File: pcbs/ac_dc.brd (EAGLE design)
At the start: 94 x 20 mm, 19 parts, among them IC1 317T, J1 22-27-2021-02, K1 G6K-2F

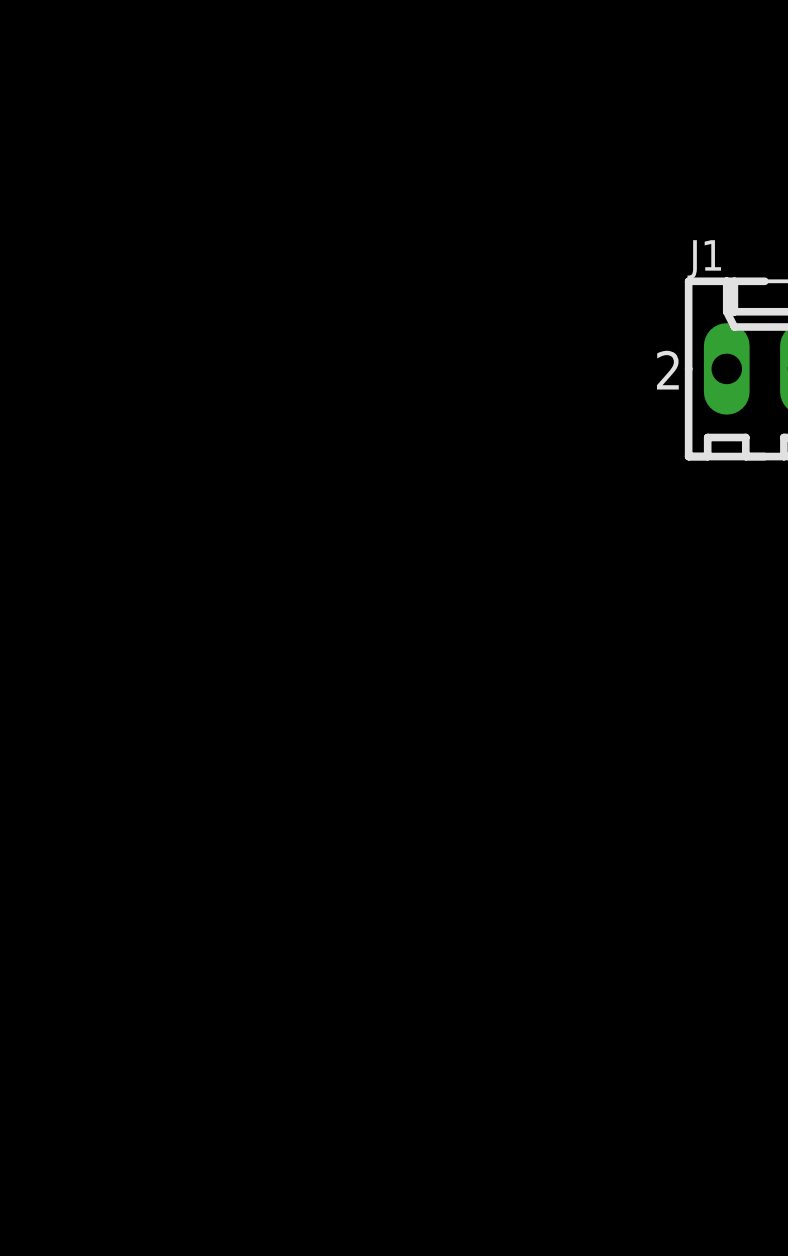
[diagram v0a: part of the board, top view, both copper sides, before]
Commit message: AC/DC: Added atmega88 and power supply.
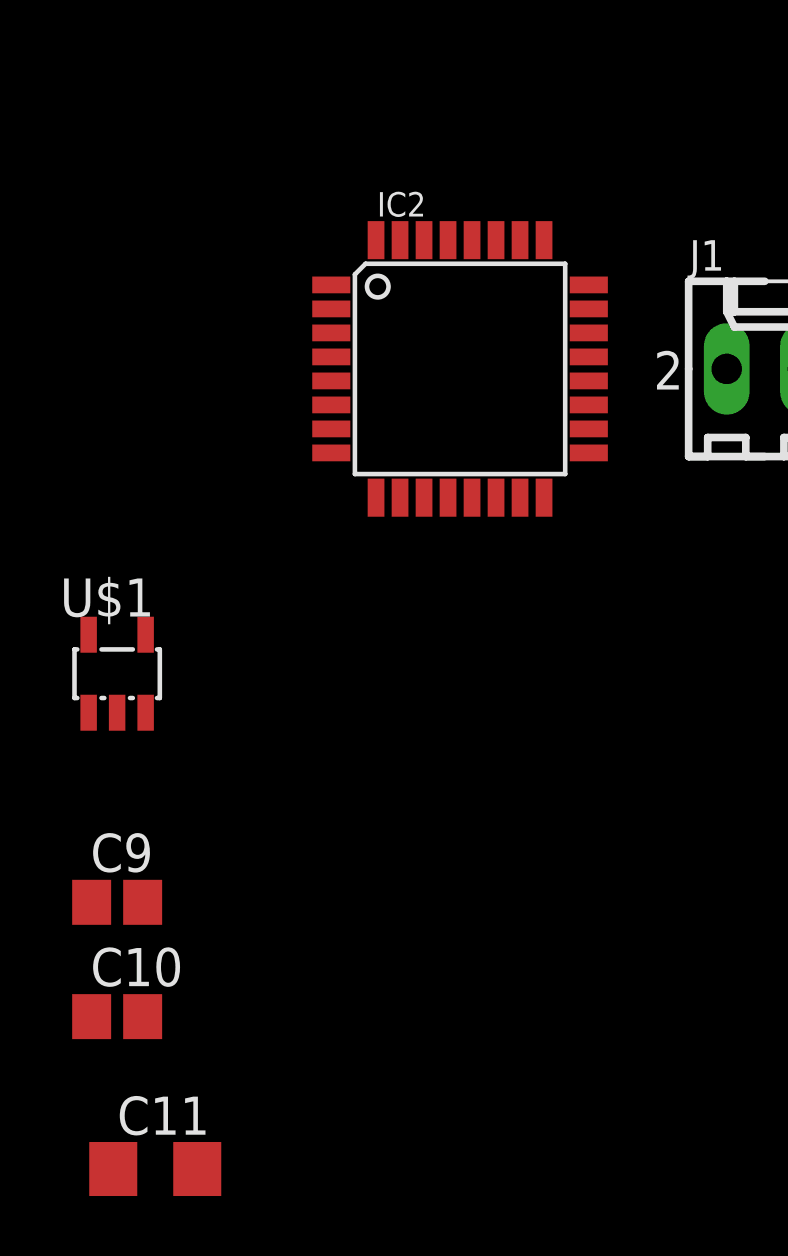
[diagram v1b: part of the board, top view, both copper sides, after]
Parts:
- added C10, C9: 100n, resistor:C0805
- added C11: 10u, resistor:C1206
- added IC2: MEGA48/88/168-AU, avr-7:TQFP32-08
- added U$1: TPS71530, ShortCircuitRobotics:SOT23-DBV
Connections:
- removed net N$15: C8.+, IC1.2
- new net +12V: C8.+, IC1.2, U$1.4
- new net VCC: C10.1, C11.1, C9.1, IC2.18, IC2.20, IC2.4, IC2.6, U$1.5
- net GND: now also C10.2, C11.2, C9.2, IC2.21, IC2.3, IC2.5, U$1.2
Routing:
- net N$15: track 13.4 -> 0.00 mm
- net +12V: track 0.00 -> 13.4 mm

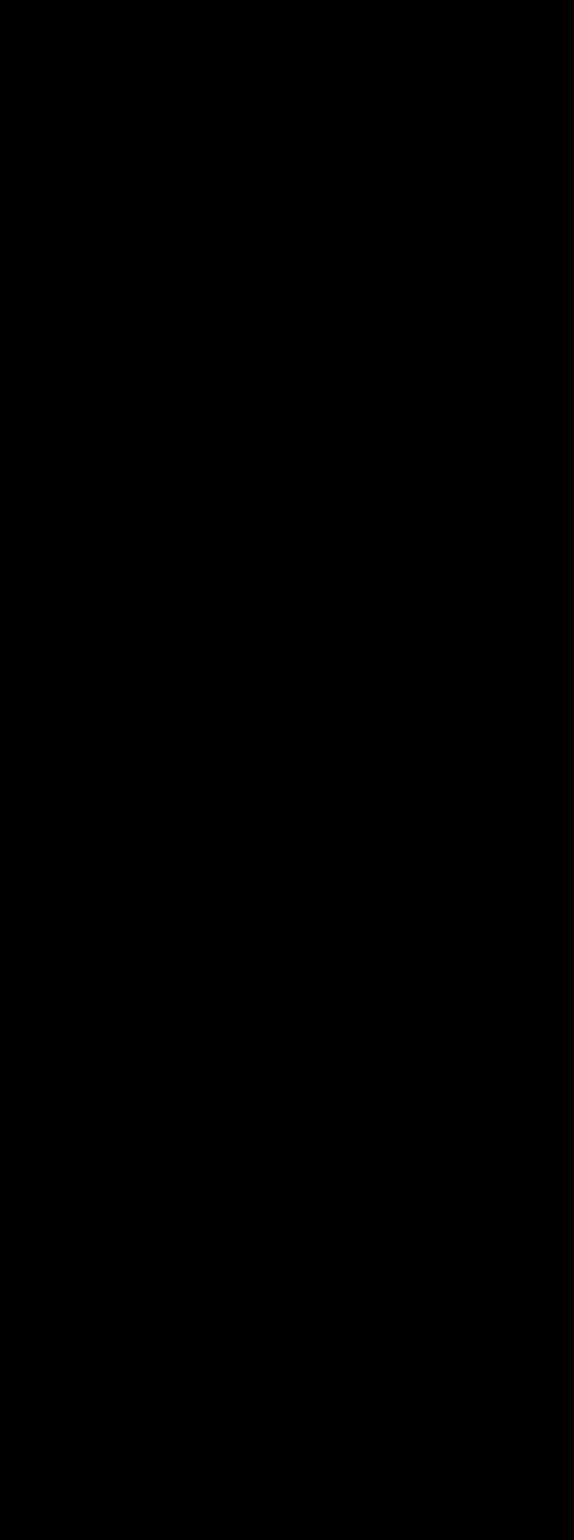
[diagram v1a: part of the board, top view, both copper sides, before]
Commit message: Main Board: Added battery connector + mosfet switch
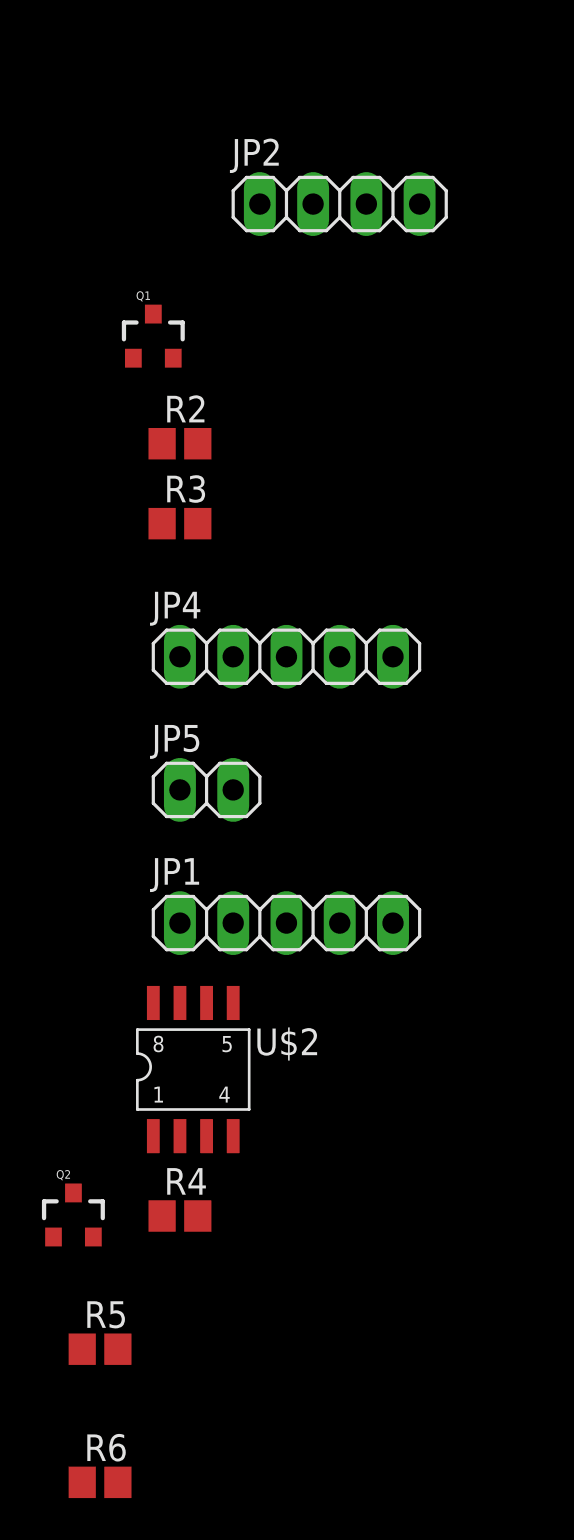
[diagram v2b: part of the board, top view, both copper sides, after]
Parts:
- added JP1, JP4: (no value), pinhead:1X05
- added JP2: (no value), pinhead:1X04
- added JP5: (no value), pinhead:1X02
- added Q1, Q2: MOSFET-NCHANNELSMD, SparkFun:SOT23-3
- added R2, R4, R5: 100k, resistor:R0805
- added R3, R6: 1k, resistor:R0805
- added U$2: IRF7416, ShortCircuitRobotics:SO8-2
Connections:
- new net BATTERY_ON: R6.1
- new net CELL_0: JP4.4
- new net CELL_1: JP4.3
- new net CELL_2: JP4.2
- new net CELL_3: JP4.1, U$2.5, U$2.6, U$2.7, U$2.8
- new net INPUT_SEL: R3.1
- new net N$11: JP1.3
- new net N$12: JP1.4
- new net N$14: K1.8, Q1.3
- new net N$15: Q1.1, R2.2, R3.2
- new net N$16: Q2.3, R4.1, U$2.4
- new net N$17: Q2.1, R5.1, R6.2
- new net N$7: JP1.2
- new net SPEED_REAR_IN: JP5.1
- new net SPEED_REAR_OUT: JP5.2
- net +12V: now also JP1.1, K1.1, R4.2, U$2.1, U$2.2, U$2.3
- net GND: now also JP1.5, JP4.5, Q1.2, Q2.2, R2.1, R5.2
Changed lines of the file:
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@@
 <element name="C10" library="resistor" package="C0805" value="100n" x="-38.1" y="-26.67"/>
 <element name="C11" library="resistor" package="C1206" value="10u" x="-36.83" y="-31.75"/>
+<element name="JP2" library="pinhead" package="1X04" value="" x="-34.29" y="-45.72"/>
+<element name="Q1" library="SparkFun" package="SOT23-3" value="MOSFET-NCHANNELSMD" x="-43.18" y="-52.07"/>
+<element name="R2" library="resistor" package="R0805" value="100k" x="-41.91" y="-57.15"/>
+<element name="R3" library="resistor" package="R0805" value="1k" x="-41.91" y="-60.96"/>
+<element name="JP4" library="pinhead" package="1X05" value="" x="-36.83" y="-67.31"/>
+<element name="JP5" library="pinhead" package="1X02" value="" x="-40.64" y="-73.66"/>
+<element name="JP1" library="pinhead" package="1X05" value="" x="-36.83" y="-80.01"/>
+<element name="U$2" library="ShortCircuitRobotics" package="SO8-2" value="IRF7416" x="-40.64" y="-87.63"/>
+<element name="R4" library="resistor" package="R0805" value="100k" x="-41.91" y="-93.98"/>
+<element name="Q2" library="SparkFun" package="SOT23-3" value="MOSFET-NCHANNELSMD" x="-46.99" y="-93.98"/>
+<element name="R5" library="resistor" package="R0805" value="100k" x="-45.72" y="-100.33"/>
+<element name="R6" library="resistor" package="R0805" value="1k" x="-45.72" y="-106.68"/>
 </elements>
 <signals>
@@
 <contactref element="C9" pad="2"/>
 <contactref element="C10" pad="2"/>
-<wire x1="46.03" y1="13.97" x2="66.88" y2="2.54" width="0" layer="19" extent="1-1"/>
-<wire x1="36.83" y1="4.74" x2="46.03" y2="13.97" width="0" layer="19" extent="1-1"/>
-<wire x1="25.4" y1="4.74" x2="36.83" y2="4.74" width="0" layer="19" extent="1-1"/>
-<wire x1="12.185" y1="3.81" x2="25.4" y2="4.74" width="0" layer="19" extent="1-1"/>
-<wire x1="12.185" y1="7.62" x2="12.185" y2="3.81" width="0" layer="19" extent="1-1"/>
-<wire x1="3.81" y1="15.24" x2="12.185" y2="7.62" width="0" layer="19" extent="1-1"/>
-<wire x1="-22.3774" y1="-4.68" x2="3.81" y2="15.24" width="0" layer="19" extent="1-1"/>
-<wire x1="-30.9626" y1="-5.48" x2="-22.3774" y2="-4.68" width="0" layer="19" extent="1-1"/>
+<contactref element="Q1" pad="2"/>
+<contactref element="R2" pad="1"/>
+<contactref element="JP1" pad="5"/>
+<contactref element="JP4" pad="5"/>
+<contactref element="Q2" pad="2"/>
+<contactref element="R5" pad="2"/>
+<wire x1="-46.04" y1="-94.98" x2="-44.87" y2="-100.33" width="0" layer="19" extent="1-1"/>
+<wire x1="-31.75" y1="-80.01" x2="-46.04" y2="-94.98" width="0" layer="19" extent="1-1"/>
+<wire x1="-31.75" y1="-67.31" x2="-31.75" y2="-80.01" width="0" layer="19" extent="1-1"/>
+<wire x1="-42.76" y1="-57.15" x2="-31.75" y2="-67.31" width="0" layer="19" extent="1-1"/>
+<wire x1="-42.23" y1="-53.07" x2="-42.76" y2="-57.15" width="0" layer="19" extent="1-1"/>
+<wire x1="-35.43" y1="-31.75" x2="-42.23" y2="-53.07" width="0" layer="19" extent="1-1"/>
+<wire x1="-37.25" y1="-26.67" x2="-35.43" y2="-31.75" width="0" layer="19" extent="1-1"/>
+<wire x1="-37.25" y1="-22.86" x2="-37.25" y2="-26.67" width="0" layer="19" extent="1-1"/>
+<wire x1="-38.1" y1="-16.54" x2="-37.25" y2="-22.86" width="0" layer="19" extent="1-1"/>
+<wire x1="-30.9626" y1="-5.48" x2="-38.1" y2="-16.54" width="0" layer="19" extent="1-1"/>
 <wire x1="-30.9626" y1="-3.88" x2="-30.9626" y2="-5.48" width="0" layer="19" extent="1-1"/>
-<wire x1="-38.1" y1="-16.54" x2="-30.9626" y2="-5.48" width="0" layer="19" extent="1-1"/>
-<wire x1="-37.25" y1="-22.86" x2="-38.1" y2="-16.54" width="0" layer="19" extent="1-1"/>
-<wire x1="-37.25" y1="-26.67" x2="-37.25" y2="-22.86" width="0" layer="19" extent="1-1"/>
-<wire x1="-35.43" y1="-31.75" x2="-37.25" y2="-26.67" width="0" layer="19" extent="1-1"/>
+<wire x1="-22.3774" y1="-4.68" x2="-30.9626" y2="-5.48" width="0" layer="19" extent="1-1"/>
+<wire x1="3.81" y1="15.24" x2="-22.3774" y2="-4.68" width="0" layer="19" extent="1-1"/>
+<wire x1="12.185" y1="7.62" x2="3.81" y2="15.24" width="0" layer="19" extent="1-1"/>
+<wire x1="12.185" y1="3.81" x2="12.185" y2="7.62" width="0" layer="19" extent="1-1"/>
+<wire x1="25.4" y1="4.74" x2="12.185" y2="3.81" width="0" layer="19" extent="1-1"/>
+<wire x1="36.83" y1="4.74" x2="25.4" y2="4.74" width="0" layer="19" extent="1-1"/>
+<wire x1="46.03" y1="13.97" x2="36.83" y2="4.74" width="0" layer="19" extent="1-1"/>
+<wire x1="66.88" y1="2.54" x2="46.03" y2="13.97" width="0" layer="19" extent="1-1"/>
 </signal>
 <signal name="N$6">
@@
 <wire x1="87.17" y1="6.35" x2="87.63" y2="5.89" width="0.8128" layer="1"/>
 <contactref element="U$1" pad="4"/>
-<wire x1="-37.15" y1="-13.94" x2="77.47" y2="2.54" width="0" layer="19" extent="1-1"/>
+<contactref element="K1" pad="1"/>
+<contactref element="JP1" pad="1"/>
+<contactref element="U$2" pad="2"/>
+<contactref element="U$2" pad="1"/>
+<contactref element="U$2" pad="3"/>
+<contactref element="R4" pad="2"/>
+<wire x1="-40.64" y1="-90.17" x2="-41.06" y2="-93.98" width="0" layer="19" extent="1-1"/>
+<wire x1="-41.91" y1="-90.17" x2="-40.64" y2="-90.17" width="0" layer="19" extent="1-1"/>
+<wire x1="-43.18" y1="-90.17" x2="-41.91" y2="-90.17" width="0" layer="19" extent="1-1"/>
+<wire x1="-41.91" y1="-80.01" x2="-41.91" y2="-90.17" width="0" layer="19" extent="1-1"/>
+<wire x1="-37.15" y1="-13.94" x2="-41.91" y2="-80.01" width="0" layer="19" extent="1-1"/>
+<wire x1="1.27" y1="-9.95" x2="-37.15" y2="-13.94" width="0" layer="19" extent="1-1"/>
+<wire x1="77.47" y1="2.54" x2="1.27" y2="-9.95" width="0" layer="19" extent="1-1"/>
+</signal>
+<signal name="N$14">
+<contactref element="K1" pad="8"/>
+<contactref element="Q1" pad="3"/>
+<wire x1="1.27" y1="-2.75" x2="-43.18" y2="-50.97" width="0" layer="19" extent="1-1"/>
+</signal>
+<signal name="N$15">
+<contactref element="Q1" pad="1"/>
+<contactref element="R3" pad="2"/>
+<contactref element="R2" pad="2"/>
+<wire x1="-41.06" y1="-57.15" x2="-41.06" y2="-60.96" width="0" layer="19" extent="1-1"/>
+<wire x1="-44.13" y1="-53.07" x2="-41.06" y2="-57.15" width="0" layer="19" extent="1-1"/>
+</signal>
+<signal name="INPUT_SEL">
+<contactref element="R3" pad="1"/>
+</signal>
+<signal name="SPEED_REAR_IN">
+<contactref element="JP5" pad="1"/>
+</signal>
+<signal name="SPEED_REAR_OUT">
+<contactref element="JP5" pad="2"/>
+</signal>
+<signal name="N$7">
+<contactref element="JP1" pad="2"/>
+</signal>
+<signal name="N$11">
+<contactref element="JP1" pad="3"/>
+</signal>
+<signal name="N$12">
+<contactref element="JP1" pad="4"/>
+</signal>
+<signal name="CELL_3">
+<contactref element="JP4" pad="1"/>
+<contactref element="U$2" pad="6"/>
+<contactref element="U$2" pad="5"/>
+<contactref element="U$2" pad="7"/>
+<contactref element="U$2" pad="8"/>
+<wire x1="-41.91" y1="-83.82" x2="-43.18" y2="-83.82" width="0" layer="19" extent="1-1"/>
+<wire x1="-40.64" y1="-83.82" x2="-41.91" y2="-83.82" width="0" layer="19" extent="1-1"/>
+<wire x1="-39.37" y1="-83.82" x2="-40.64" y2="-83.82" width="0" layer="19" extent="1-1"/>
+<wire x1="-41.91" y1="-67.31" x2="-41.91" y2="-83.82" width="0" layer="19" extent="1-1"/>
+</signal>
+<signal name="N$16">
+<contactref element="R4" pad="1"/>
+<contactref element="U$2" pad="4"/>
+<contactref element="Q2" pad="3"/>
+<wire x1="-42.76" y1="-93.98" x2="-46.99" y2="-92.88" width="0" layer="19" extent="1-1"/>
+<wire x1="-39.37" y1="-90.17" x2="-42.76" y2="-93.98" width="0" layer="19" extent="1-1"/>
+</signal>
+<signal name="N$17">
+<contactref element="R5" pad="1"/>
+<contactref element="Q2" pad="1"/>
+<contactref element="R6" pad="2"/>
+<wire x1="-46.57" y1="-100.33" x2="-44.87" y2="-106.68" width="0" layer="19" extent="1-1"/>
+<wire x1="-47.94" y1="-94.98" x2="-46.57" y2="-100.33" width="0" layer="19" extent="1-1"/>
+</signal>
+<signal name="BATTERY_ON">
+<contactref element="R6" pad="1"/>
+</signal>
+<signal name="CELL_0">
+<contactref element="JP4" pad="4"/>
+</signal>
+<signal name="CELL_1">
+<contactref element="JP4" pad="3"/>
+</signal>
+<signal name="CELL_2">
+<contactref element="JP4" pad="2"/>
 </signal>
 </signals>
